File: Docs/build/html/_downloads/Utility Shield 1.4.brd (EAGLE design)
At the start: 40.6 x 53.3 mm, 15 parts, among them U2 MCP73831

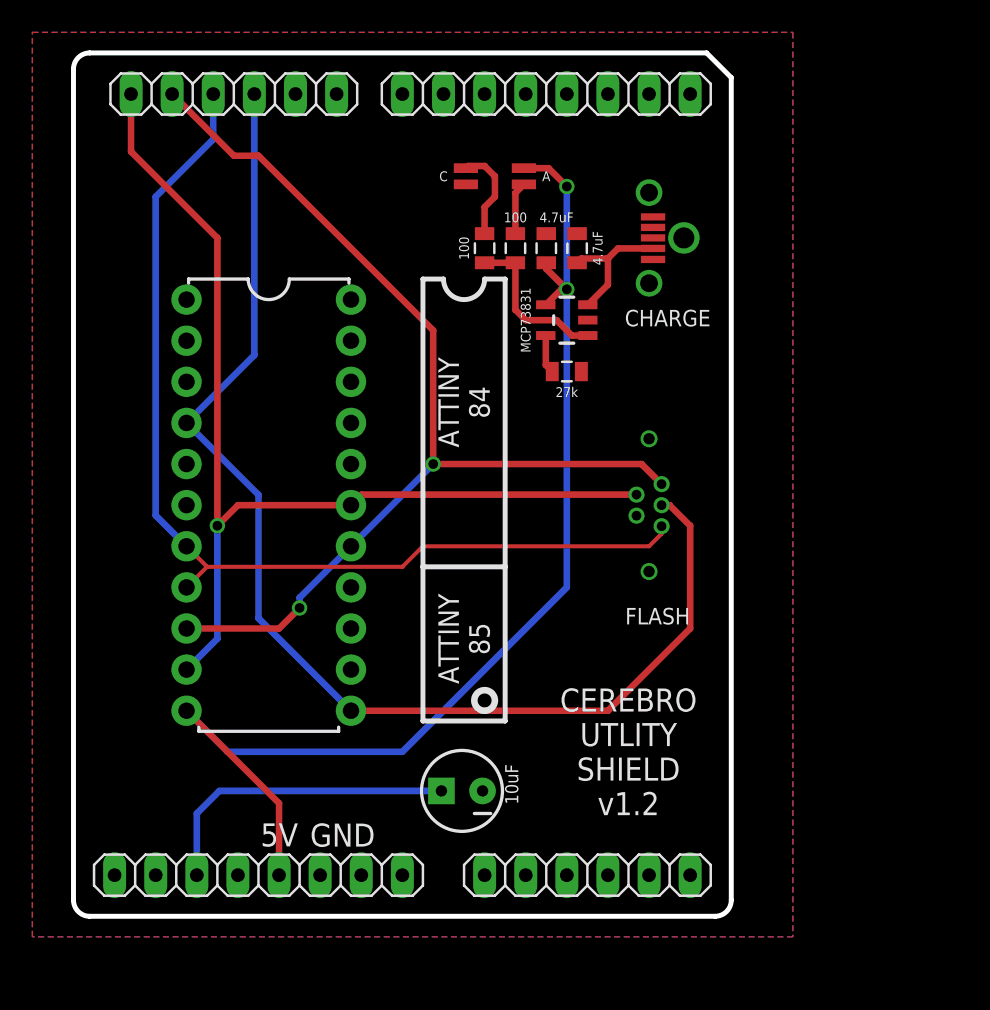
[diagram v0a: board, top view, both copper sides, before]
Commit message: Charging Dock and Utility Shield revisions. Doc Update
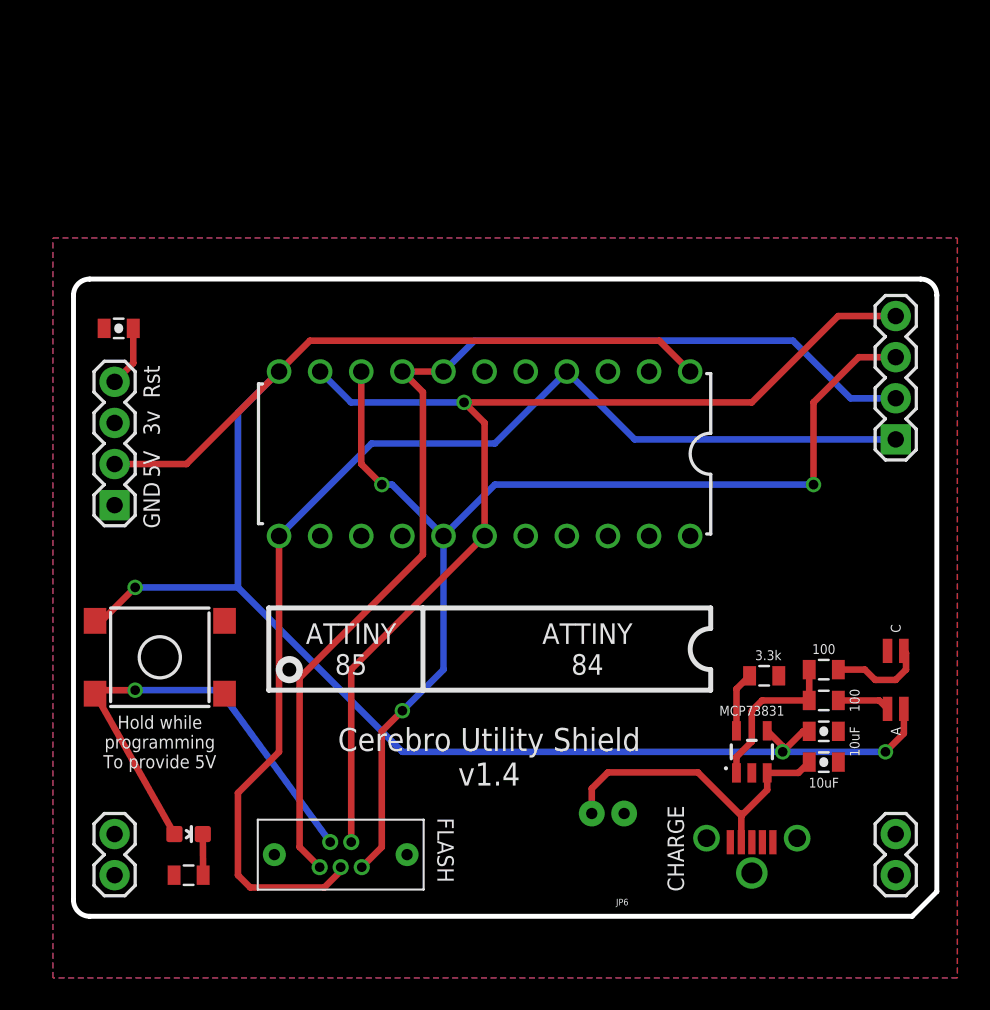
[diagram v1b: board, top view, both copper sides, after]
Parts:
- removed AD, AD1: 6x1F-H8.5, SmartPrj:1X06
- removed C1: 10uF, SparkFun-Passives:CPOL-RADIAL-10UF-25V
- removed IOL, POWER: 8x1F-H8.5, SmartPrj:1X08
- added C4: 10uF, SparkFun-Capacitors:0805-CAP
- added JP2, JP4: (no value), SparkFun-Connectors:1X02
- added JP3, JP5: (no value), SparkFun-Connectors:1X04
- added JP6: (no value), SparkFun-Connectors:JST-2-PTH-NS
- added LED1: (no value), Andy-library:LED-0603
- added R4: 20k, Andy-library:0805
- added S1: TAC_SWITCHSMD, Andy-library:TACTILE-SWITCH-SMD
- C2, C3: value 4.7uF -> 10uF; device SparkFun-Capacitors:0805 -> SparkFun-Capacitors:0805-CAP
- R3: value 27k -> 3.3k
- moved U$2 39.8 mm to (50.8, 14.6), turned to 270 degrees
- moved U$3 37.6 mm to (41.9, 4.83), turned to 0 degrees
- moved C2 35.2 mm to (46.4, 9.53), turned to 0 degrees
- moved C3 34.4 mm to (46.4, 11.4), turned to 0 degrees
- moved R1 33.8 mm to (46.4, 13.3), turned to 180 degrees
- moved R2 33.4 mm to (46.4, 15.2), turned to 180 degrees
- moved U2 29.0 mm to (41.9, 10.2), turned to 0 degrees
- moved JP1 28.8 mm to (16.5, 3.81), flipped to the bottom, turned to 0 degrees
- moved R3 22.4 mm to (42.7, 14.9)
- moved U$1 13.7 mm to (25.4, 28.6), turned to 180 degrees
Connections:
- new net N$2: LED1.C, R4.1
- new net N$7: JP1.4, LED1.A, S1.3
- net 3VDC: now also JP3.3; no longer POWER.4
- net 5VDC: now also JP3.2, S1.1, U$1.1; no longer POWER.5
- net GND: now also C4.1, JP3.1, JP6.1, R4.2; no longer C1.2, JP1.4, POWER.6, POWER.7
- net MISO: now also JP5.3; no longer AD1.5
- net MOSI: now also JP5.2; no longer AD1.4
- net N$1: now also C4.2, JP3.4; no longer C1.1, POWER.3
- net N$9: now also JP6.2
- net RST: now also JP5.1; no longer AD1.3
- net SCK: now also JP5.4; no longer AD1.6
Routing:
- net 5VDC: track 73.0 -> 114.8 mm, vias 2 -> 3
- net N$7: track 0.00 -> 29.3 mm, vias 0 -> 1
- net N$1: track 19.5 -> 3.78 mm
- net N$9: track 8.44 -> 20.3 mm
- net MISO: track 64.9 -> 70.7 mm, vias 2 -> 3
- net SCK: track 65.2 -> 69.7 mm
- net MOSI: track 63.2 -> 67.6 mm
- net N$2: track 0.00 -> 2.54 mm
- net RST: track 75.7 -> 73.4 mm
- net N$6: track 2.39 -> 3.74 mm
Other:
- board size 40.6 x 53.3 mm -> 53.3 x 39.4 mm
- board text added: "3v"
- board text added: "Cerebro Utility Shield v1.4"
- board text added: "Hold while programming To provide 5V"
- board text added: "Rst"
- board text removed: "CEREBRO UTLITY SHIELD v1.2"
